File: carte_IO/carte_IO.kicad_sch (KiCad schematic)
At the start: 27 parts, among them J1 AX12, J10 AX12, J2 Conn_01x02_Pin, J3 Conn_01x02_Pin, J4 Conn_01x02_Pin, J5 Conn_01x02_Pin, J6 Conn_01x02_Pin, J7 Conn_01x02_Pin, J8 Conn_01x02_Pin, J9 Conn_01x02_Pin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

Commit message: quelques connections
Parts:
- removed J1: AX12, symbol Connector:Conn_01x03_Pin
- added J11: AX12, symbol Connector:Conn_01x04_Pin
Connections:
- net +5V: now also J10.1 (Pin_1), J11.1 (Pin_1)
- net GND: now also J10.2 (Pin_2), U1.1 (GND), U1.27 (GND), U1.39 (GND), U1.61 (GND), U1.62 (GND), U1.74 (GND), J11.2 (Pin_2)
- net SCL: now also U1.46 (19_A5_SCL0_Touch)
- net SDA: now also U1.45 (18_A4_SDA0_Touch)
- net AX12: now reaches J10.3 (Pin_3)
- net +3.3V: now reaches U1.15 (3.3V)
- net +3.3V: now also U1.26 (3.3V), U1.75 (3.3V)
- new net RX: J11.4 (Pin_4)
- new net TX: J11.3 (Pin_3)
- no-connect marks 6 -> 7
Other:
- note added: "AX12"
- note added: "CAPTEURS"
- note added: "SERVOMOTEURS"
- moved on the sheet: J10, J8, J9

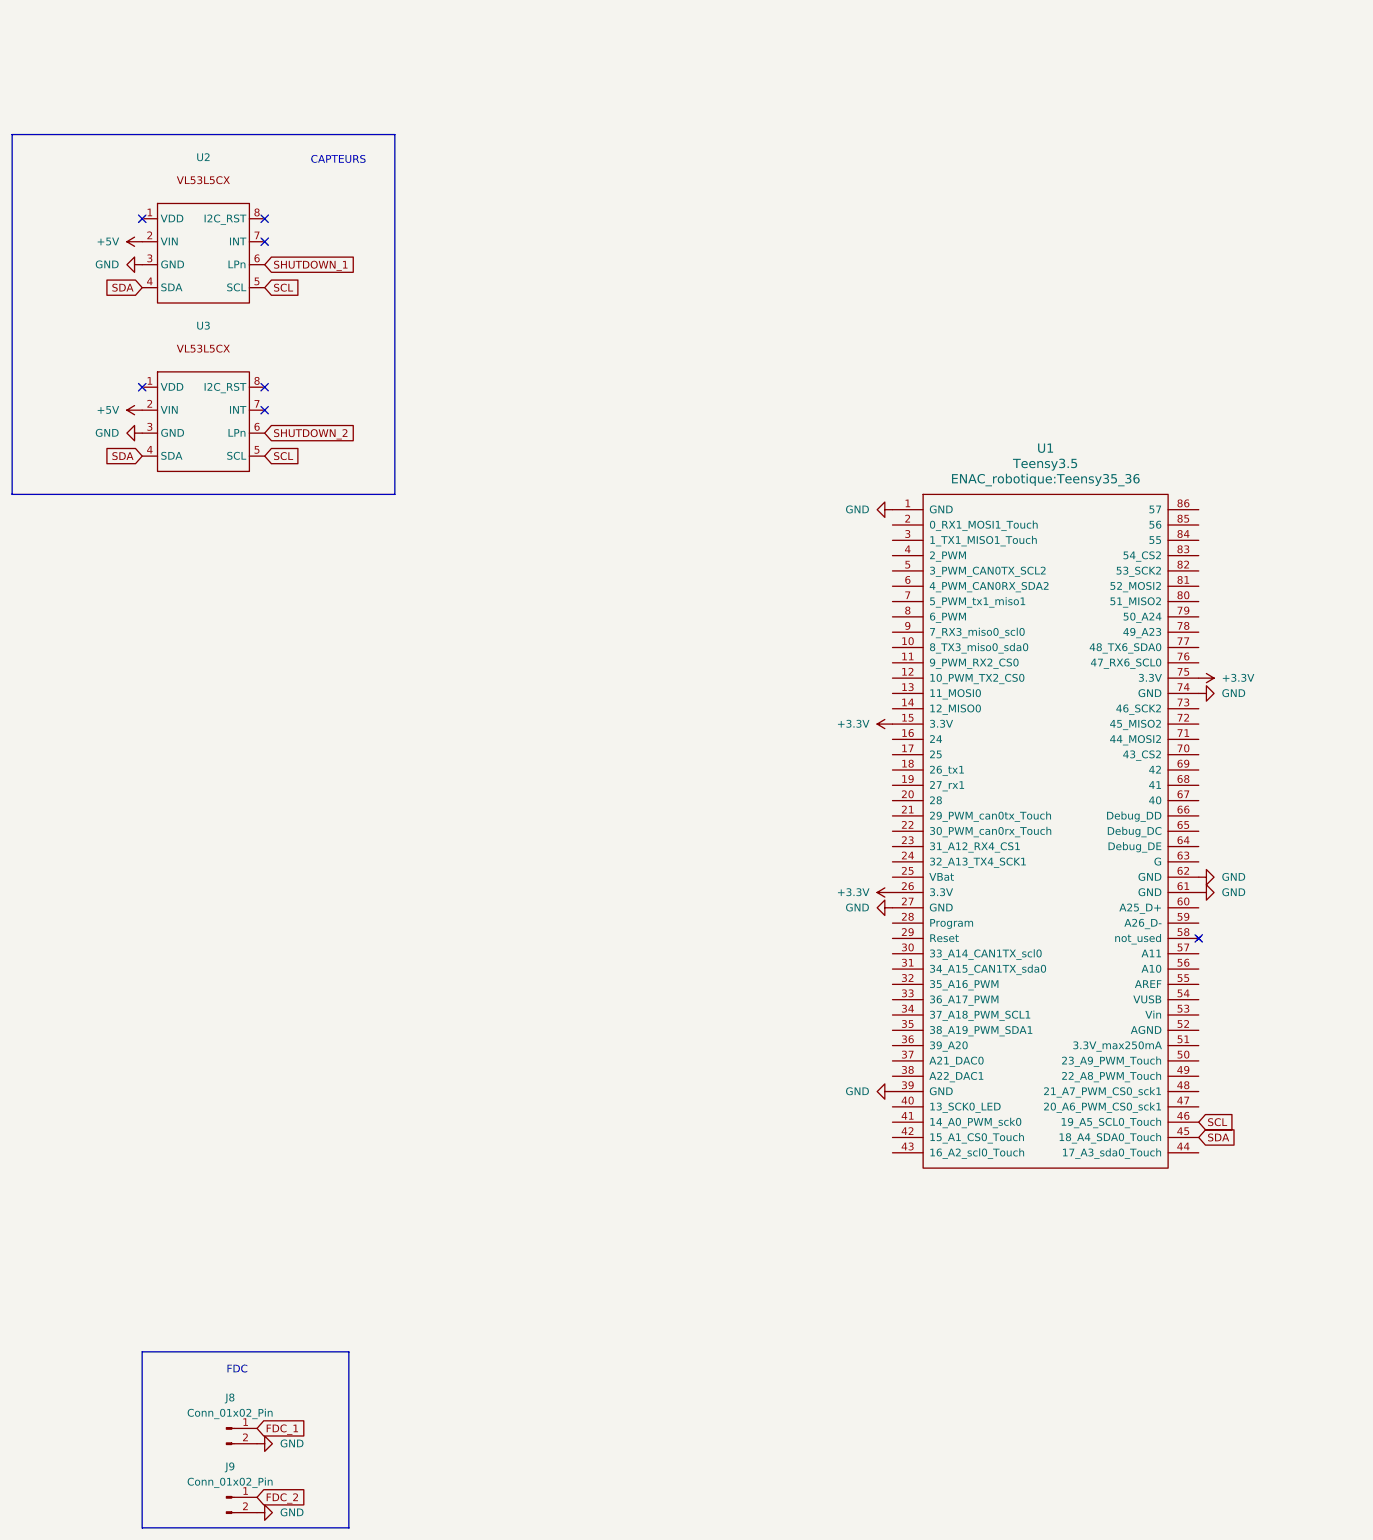
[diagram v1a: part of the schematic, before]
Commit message: move to lk32KC & add gitignore
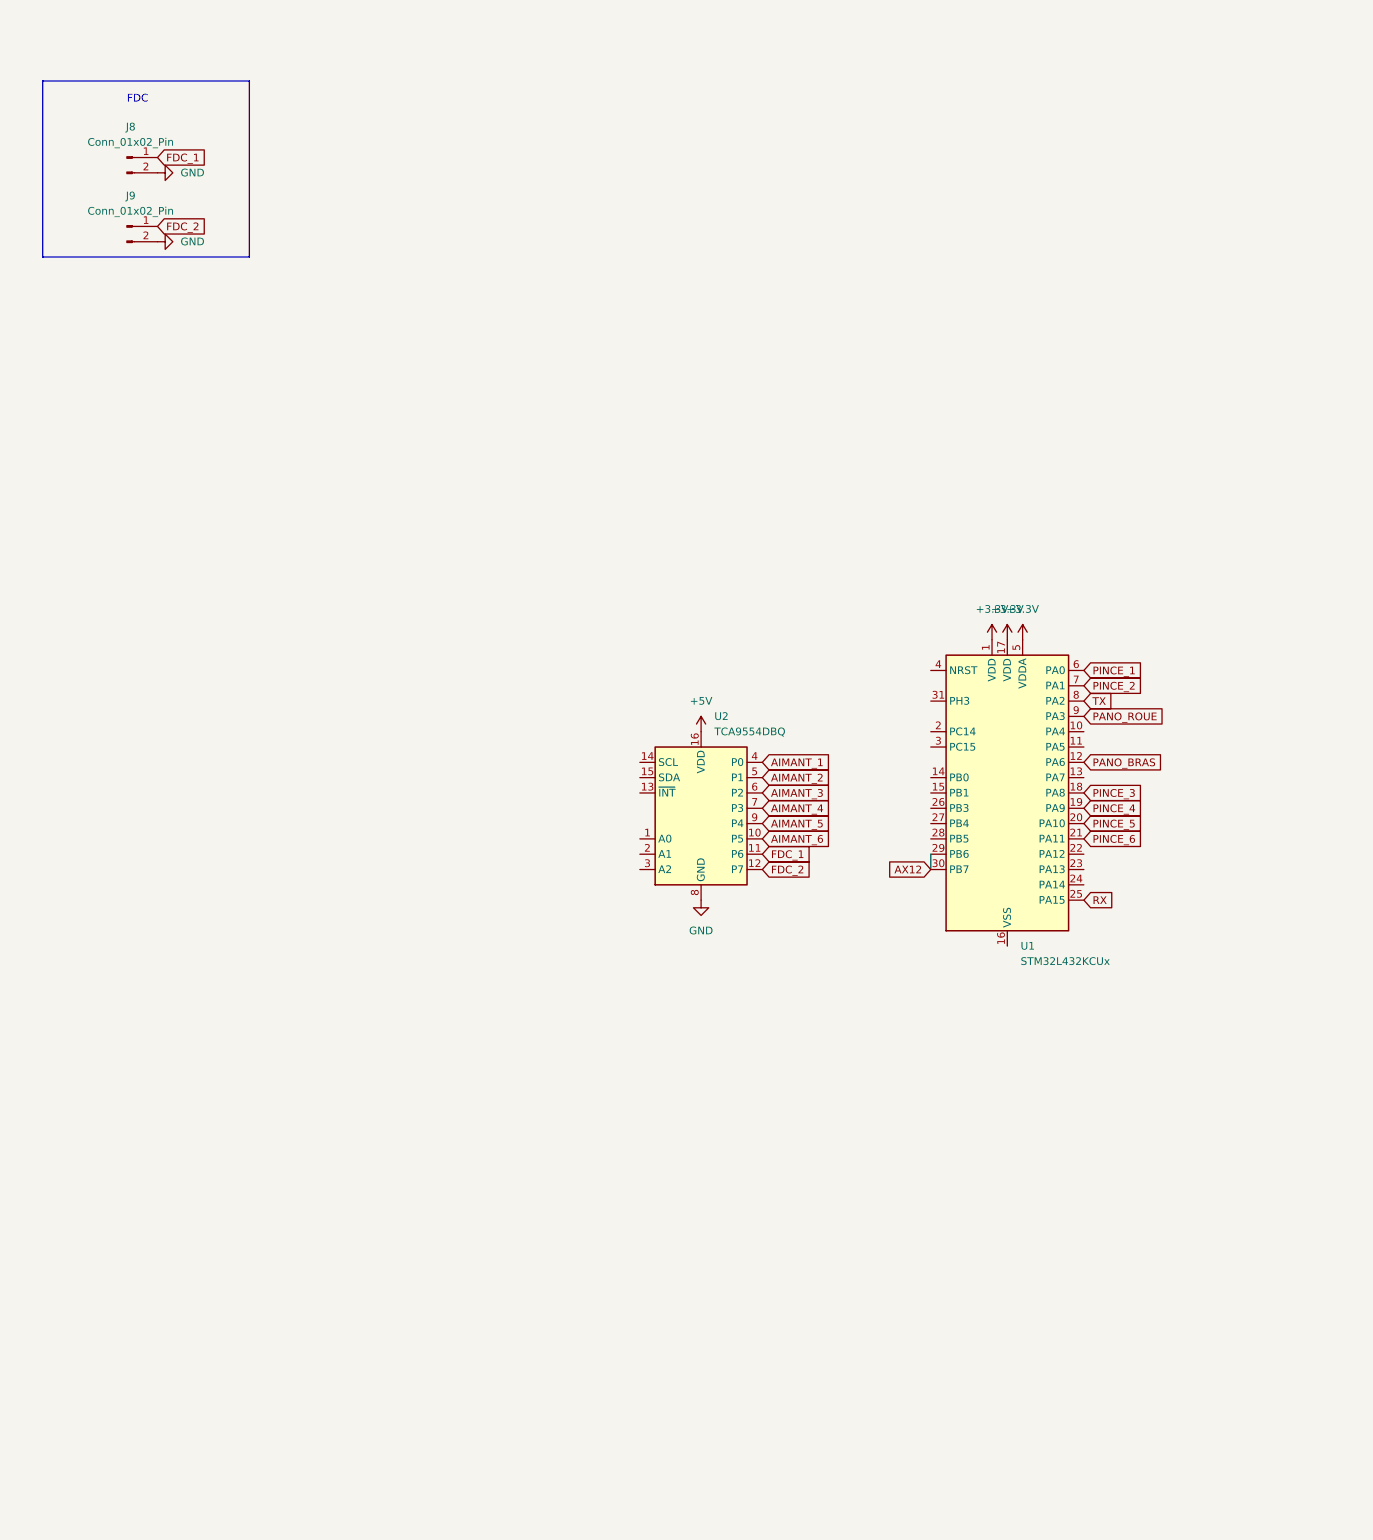
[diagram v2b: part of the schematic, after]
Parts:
- removed U1: Teensy3.5, ENAC_robotique:Teensy35_36, symbol ENAC_robotique:Teensy3.5
- removed U2, U3: ~, symbol ENAC_robotique:VL53L5CX
- added U1: STM32L432KCUx, Package_DFN_QFN:QFN-32-1EP_5x5mm_P0.5mm_EP3.45x3.45mm, symbol MCU_ST_STM32L4:STM32L432KCUx
- added U2: TCA9554DBQ, Package_SO:SSOP-16_3.9x4.9mm_P0.635mm, symbol Interface_Expansion:TCA9554DBQ
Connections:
- net +3.3V: now also U1.1 (VDD), U1.17 (VDD), U1.5 (VDDA)
- net +5V: now also U2.16 (VDD)
- net AIMANT_1: now also U2.4 (P0)
- net AIMANT_2: now also U2.5 (P1)
- net AIMANT_3: now also U2.6 (P2)
- net AIMANT_4: now also U2.7 (P3)
- net AIMANT_5: now also U2.9 (P4)
- net AIMANT_6: now also U2.10 (P5)
- net AX12: now also U1.29 (PB6), U1.30 (PB7)
- net FDC_1: now also U2.11 (P6)
- net FDC_2: now also U2.12 (P7)
- net GND: now also U2.8 (GND)
- net PANO_BRAS: now also U1.12 (PA6)
- net PANO_ROUE: now also U1.9 (PA3)
- net PINCE_1: now also U1.6 (PA0)
- net PINCE_2: now also U1.7 (PA1)
- net PINCE_3: now also U1.18 (PA8)
- net PINCE_4: now also U1.19 (PA9)
- net PINCE_5: now also U1.20 (PA10)
- net PINCE_6: now also U1.21 (PA11)
- net RX: now also U1.25 (PA15)
- net TX: now also U1.8 (PA2)
- new net: U1.16 (VSS), U1.32 (VSS), U1.33 (VSS)
- no-connect marks 7 -> 0
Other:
- note removed: "CAPTEURS"
- moved on the sheet: J8, J9

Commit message: some instructions
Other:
- note added: "INSTRUCTIONS ( à réaliser dans l'ordre ) : 1) Rajouter des pulls down (environ10k) sur la gate des transistors. 2) Brancher les aimant entre le +12V et le Drain des mosfets. 3) Mettre une empreinte pour la pin de l'AX12. 4) Choisir un Régulateur 12V-?A et le placer avec ses capacité de découplage ( voir datasheet ) 5) Choisir un régulateur 3.3V-?A et le placer avec ses capacité de découplage ( vo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"
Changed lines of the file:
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@@
   (junction (at 322.58 217.17) (diameter 0) (color 0 0 0 0)
   )
+  (junction (at 196.85 161.29) (diameter 0) (color 0 0 0 0)
+  )
   (junction (at 322.58 231.14) (diameter 0) (color 0 0 0 0)
   )
@@
   (junction (at 325.12 184.15) (diameter 0) (color 0 0 0 0)
   )
+  (junction (at 210.82 123.19) (diameter 0) (color 0 0 0 0)
+  )
   (junction (at 372.11 207.01) (diameter 0) (color 0 0 0 0)
   )
@@
     (stroke (width 0) (type default))
   )
+  (wire (pts (xy 210.82 121.92) (xy 210.82 123.19))
+    (stroke (width 0) (type default))
+  )
   (wire (pts (xy 314.96 217.17) (xy 322.58 217.17))
     (stroke (width 0) (type default))
@@
     (stroke (width 0) (type default))
   )
+  (wire (pts (xy 196.85 162.56) (xy 198.12 162.56))
+    (stroke (width 0) (type default))
+  )
+  (wire (pts (xy 196.85 161.29) (xy 196.85 162.56))
+    (stroke (width 0) (type default))
+  )
   (wire (pts (xy 331.47 184.15) (xy 331.47 189.23))
     (stroke (width 0) (type default))
   )
-  (wire (pts (xy 198.12 160.02) (xy 198.12 162.56))
+  (wire (pts (xy 196.85 160.02) (xy 196.85 161.29))
+    (stroke (width 0) (type default))
+  )
+  (wire (pts (xy 213.36 124.46) (xy 213.36 123.19))
+    (stroke (width 0) (type default))
+  )
+  (wire (pts (xy 195.58 161.29) (xy 196.85 161.29))
     (stroke (width 0) (type default))
   )
@@
     (stroke (width 0) (type default))
   )
+  (wire (pts (xy 208.28 123.19) (xy 210.82 123.19))
+    (stroke (width 0) (type default))
+  )
+  (wire (pts (xy 208.28 124.46) (xy 208.28 123.19))
+    (stroke (width 0) (type default))
+  )
+  (wire (pts (xy 210.82 123.19) (xy 210.82 124.46))
+    (stroke (width 0) (type default))
+  )
   (wire (pts (xy 325.12 184.15) (xy 331.47 184.15))
     (stroke (width 0) (type default))
@@
     (stroke (width 0) (type default))
   )
+  (wire (pts (xy 213.36 123.19) (xy 210.82 123.19))
+    (stroke (width 0) (type default))
+  )
   (wire (pts (xy 331.47 195.58) (xy 331.47 191.77))
     (stroke (width 0) (type default))
@@
   )
   (wire (pts (xy 314.96 215.9) (xy 314.96 217.17))
+    (stroke (width 0) (type default))
+  )
+  (wire (pts (xy 196.85 160.02) (xy 198.12 160.02))
     (stroke (width 0) (type default))
   )
@@
     (effects (font (size 1.27 1.27)) (justify left bottom))
   )
+  (text "INSTRUCTIONS ( à réaliser dans l'ordre ) : \n1) Rajouter des pulls down (environ10k) sur la gate des transistors.\n2) Brancher les aimant entre le +12V et le Drain des mosfets.\n3) Mettre une empreinte pour la pin de l'AX12.\n4) Choisir un Régulateur 12V-?A et le placer avec ses capacité de découplage ( voir datasheet )\n5) Choisir un régulateur 3.3V-?A et le placer avec ses capacité de découplage ( voir datasheet )\nAttention au courant ! \n6) Ajouter un Bornier d'alimentation (Voir lib custom)\n\nPour les composant passif ! :\nLes empreintes des Résistance et des condensateur sont des SMD \nen Metric 0603. Il faut regarder le 4 premiers chiffres et ne \npas prendre celle avec écrit \"pad\"\nexemple dans la bibliothèque d'empreinte : \nle 0603 est \"R_0603_1608Metric\" et est différent du 0201 \"R_0201_0603Metric\" \n\nEnsuite ( déjà si le reste est fait c'est déjà bien ): \nDans le PCB editor placer les composants. (Ne faite pas le routage !)\nPlacez les en essayant de visualiser les pistes qui vont être reliée. \nLimitez les croisements et échanger des pins qui ont les même fonctions si nécéssaire.\n\nSi certaines choses ne sont pas claires les questions ça existe :) ( et discord aussi )"
+    (at 21.59 274.32 0)
+    (effects (font (size 3 3)) (justify left bottom))
+  )
   (text "UART COM" (at 341.63 142.24 0)
     (effects (font (size 1.27 1.27)) (justify left bottom))
@@
     )
   )
-  (global_label "AX12" (shape input) (at 198.12 162.56 180) (fields_autoplaced)
-    (effects (font (size 1.27 1.27)) (justify right))
-    (property "Intersheetrefs" "${INTERSHEET_REFS}" (at 190.4177 162.56 0)
+  (global_label "AX12" (shape input) (at 195.58 161.29 180) (fields_autoplaced)
+    (effects (font (size 1.27 1.27)) (justify right))
+    (property "Intersheetrefs" "${INTERSHEET_REFS}" (at 187.8777 161.29 0)
       (effects (font (size 1.27 1.27)) (justify right) hide)
     )
@@
         (path "/cff6ead8-7e4b-448f-a3de-63b4a72a1d61"
           (reference "#PWR012") (unit 1)
-        )
-      )
-    )
-  )
-  (symbol (lib_id "power:+3.3V") (at 213.36 124.46 0) (unit 1)
-    (in_bom yes) (on_board yes) (dnp no) (fields_autoplaced)
-    (property "Reference" "#PWR030" (at 213.36 128.27 0)
-      (effects (font (size 1.27 1.27)) hide)
-    )
-    (property "Value" "+3.3V" (at 213.36 119.38 0)
-      (effects (font (size 1.27 1.27)))
-    )
-    (property "Footprint" "" (at 213.36 124.46 0)
-      (effects (font (size 1.27 1.27)) hide)
-    )
-    (property "Datasheet" "" (at 213.36 124.46 0)
-      (effects (font (size 1.27 1.27)) hide)
-    )
-    (pin "1")
-    (instances
-      (project "carte_IO"
-        (path "/cff6ead8-7e4b-448f-a3de-63b4a72a1d61"
-          (reference "#PWR030") (unit 1)
         )
       )
@@
         (path "/cff6ead8-7e4b-448f-a3de-63b4a72a1d61"
           (reference "J5") (unit 1)
-        )
-      )
-    )
-  )
-  (symbol (lib_id "power:+3.3V") (at 208.28 124.46 0) (unit 1)
-    (in_bom yes) (on_board yes) (dnp no) (fields_autoplaced)
-    (property "Reference" "#PWR032" (at 208.28 128.27 0)
-      (effects (font (size 1.27 1.27)) hide)
-    )
-    (property "Value" "+3.3V" (at 208.28 119.38 0)
-      (effects (font (size 1.27 1.27)))
-    )
-    (property "Footprint" "" (at 208.28 124.46 0)
-      (effects (font (size 1.27 1.27)) hide)
-    )
-    (property "Datasheet" "" (at 208.28 124.46 0)
-      (effects (font (size 1.27 1.27)) hide)
-    )
-    (pin "1")
-    (instances
-      (project "carte_IO"
-        (path "/cff6ead8-7e4b-448f-a3de-63b4a72a1d61"
-          (reference "#PWR032") (unit 1)
         )
       )
@@
     )
   )
-  (symbol (lib_id "power:+3.3V") (at 210.82 124.46 0) (unit 1)
-    (in_bom yes) (on_board yes) (dnp no) (fields_autoplaced)
-    (property "Reference" "#PWR031" (at 210.82 128.27 0)
-      (effects (font (size 1.27 1.27)) hide)
-    )
-    (property "Value" "+3.3V" (at 210.82 119.38 0)
-      (effects (font (size 1.27 1.27)))
-    )
-    (property "Footprint" "" (at 210.82 124.46 0)
-      (effects (font (size 1.27 1.27)) hide)
-    )
-    (property "Datasheet" "" (at 210.82 124.46 0)
-      (effects (font (size 1.27 1.27)) hide)
-    )
+  (symbol (lib_id "power:+3.3V") (at 210.82 121.92 0) (unit 1)
+    (in_bom yes) (on_board yes) (dnp no)
+    (property "Reference" "#PWR031" (at 210.82 125.73 0)
+      (effects (font (size 1.27 1.27)) hide)
+    )
+    (property "Value" "+3.3V" (at 204.47 119.38 0)
+      (effects (font (size 1.27 1.27)))
+    )
+    (property "Footprint" "" (at 210.82 121.92 0)
+      (effects (font (size 1.27 1.27)) hide)
+    )
+    (property "Datasheet" "" (at 210.82 121.92 0)
+      (effects (font (size 1.27 1.27)) hide)
+    )
